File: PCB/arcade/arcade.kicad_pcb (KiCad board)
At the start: 2 copper layers, 146.3 x 55.8 mm, 55 parts, among them J1 USB_C_Receptacle_USB2.0_16P, J10 USB_A, J11 USB_A, J15 Conn_02x24_Odd_Even, J16 Conn_02x24_Odd_Even, J2 Conn_02x03_Odd_Even, J3 Conn_02x06_Odd_Even, J4 Screw_Terminal_01x02, J5 Screw_Terminal_01x12, J6 Screw_Terminal_01x08, J7 Screw_Terminal_01x12, J8 Conn_01x02_Pin, J9 Conn_01x06_Pin, U1 RP2040, U2 TLC5947RHB, U3 TLC5947RHB, U4 TLC5947RHB, U5 ME6211C33M5, U6 CD74HC4067M, U7 CD74HC4067M, U8 W25Q16JVSS, U9 FE1.1s, Y2 Crystal_GND24, Y3 Crystal_GND24

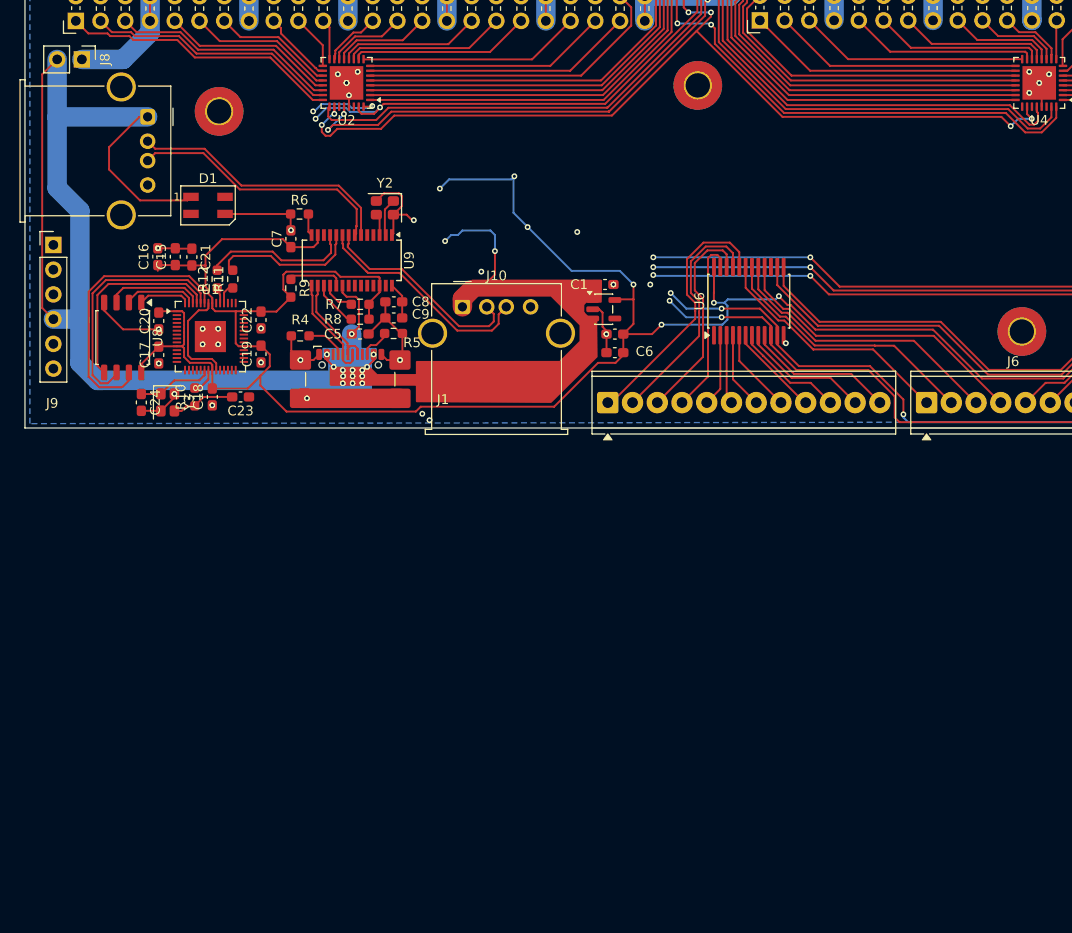
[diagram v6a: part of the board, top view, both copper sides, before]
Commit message: refactored gamepads
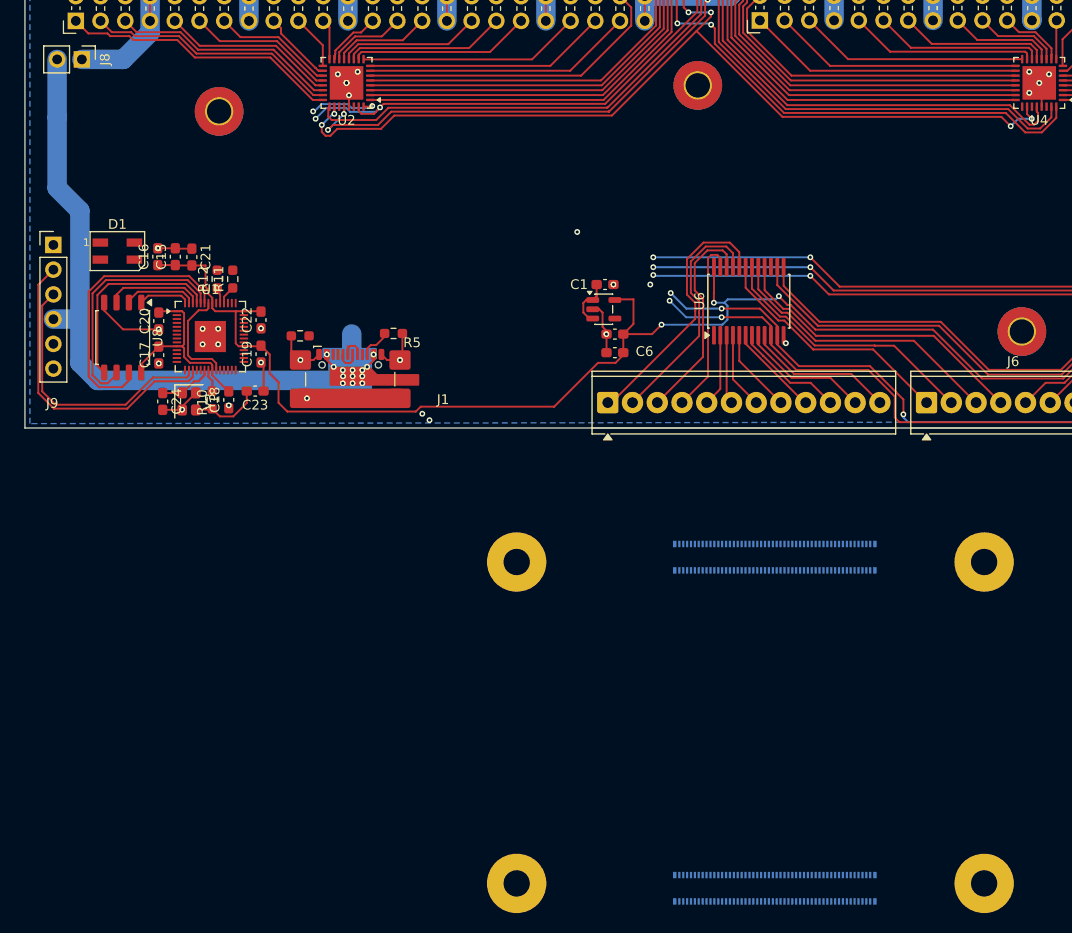
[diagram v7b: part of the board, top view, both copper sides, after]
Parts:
- removed C5, C7, C8, C9: 22pf, Capacitor_SMD:C_0603_1608Metric_Pad1.08x0.95mm_HandSolder
- removed J10, J11: USB_A, Connector_USB:USB_A_Molex_67643_Horizontal
- removed R6, R7, R8, R9: 5.1k, Resistor_SMD:R_0603_1608Metric_Pad0.98x0.95mm_HandSolder
- removed U9: FE1.1s, Package_SO:SSOP-28_3.9x9.9mm_P0.635mm
- removed Y2: Crystal_GND24, Crystal:Crystal_SMD_2520-4Pin_2.5x2.0mm
- added H5: ~, Raspberry-Pi-CM5:RaspberryPi-CM5-Module-Pad, F.Cu at (99.8, 125.5)
- moved D1 10.4 mm to (32.4, 97.0)
- moved C24 2.20 mm to (37.0, 112.5)
- moved Y3 2.20 mm to (39.7, 112.5)
- moved R10 1.81 mm to (42.1, 112.3)
- moved C18 1.71 mm to (43.8, 112.3)
- moved C23 1.62 mm to (46.5, 111.4)
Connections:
- J9 pad 2: /RXD0 -> /RX0
- J9 pad 3: /TXD0 -> /TX0
- U1 pad 16: unconnected-(U1-GPIO13-Pad16) -> /TX0
- U1 pad 17: unconnected-(U1-GPIO14-Pad17) -> /RX0
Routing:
- net /VBUS: track 147.0 -> 57.7 mm, vias 16 -> 13
- net /3.3v: track 254.6 -> 183.7 mm, vias 8 -> 4
- net /RX0: track 0.00 -> 31.9 mm
- net /TX0: track 0.00 -> 27.9 mm
- net /D3-: track 27.5 -> 0.00 mm
- net /D3+: track 26.9 -> 0.00 mm
- net /D2+: track 23.2 -> 0.00 mm
- net /GND: track 71.6 -> 49.4 mm, vias 36 -> 33
- net /D2-: track 21.6 -> 0.00 mm
- net /D1+: track 15.3 -> 0.00 mm
- net /D1-: track 14.9 -> 0.00 mm
- net /DU-: track 10.9 -> 2.46 mm
- net /DU+: track 10.9 -> 3.30 mm
- net Net-(U9-BUSJ): track 5.54 -> 0.00 mm
- net Net-(U9-~{XRSTJ}): track 4.75 -> 0.00 mm
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
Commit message: board
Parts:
- removed H5: ~, Raspberry-Pi-CM5:RaspberryPi-CM5-Module-Pad
- added Module1: ComputeModule5-CM5, Raspberry Pi CM5:Raspberry-Pi-5-Compute-Module, B.Cu at (86.4, 104.4)
- added U9: TS3USB221ARSERG4, TS3USB221A:RSE10, F.Cu at (55.8, 101.5)
- moved H3 73.1 mm to (160.8, 104.7)
- moved H1 56.8 mm to (68.5, 108.9)
- moved H2 12.6 mm to (34.1, 73.6)
- moved J2 7.91 mm to (159.8, 65.5)
- moved J4 7.91 mm to (163.0, 76.7)
- moved U2 7.91 mm to (54.5, 72.0)
- moved U3 7.91 mm to (91.0, 57.8)
- moved U4 7.91 mm to (125.6, 72.0)
- moved J15 7.91 mm to (26.7, 65.6)
- moved J8 7.91 mm to (27.3, 69.6)
- moved J16 7.91 mm to (96.9, 65.6)
- moved U5 7.67 mm to (74.6, 103.2)
- moved C1 7.67 mm to (74.8, 100.7)
- moved C2 7.67 mm to (75.8, 105.7)
- moved C6 7.67 mm to (75.8, 107.7)
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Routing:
- net Net-(J15-Pin_34): track 61.0 -> 69.6 mm
- net /VBUS: track 57.7 -> 66.0 mm
- net Net-(J6-Pin_6): track 23.0 -> 30.8 mm
- net Net-(J6-Pin_5): track 26.4 -> 34.2 mm
- net Net-(J6-Pin_7): track 20.2 -> 27.3 mm
- net /IO41: track 101.3 -> 108.4 mm
- net /EXT_5V: track 358.6 -> 365.7 mm
- net Net-(U2-SOUT): track 49.5 -> 56.6 mm
- net /3.3v: track 183.7 -> 177.0 mm, vias 4 -> 3
- net Net-(J16-Pin_37): track 17.4 -> 22.1 mm
- net /PD6: track 59.9 -> 56.9 mm
- net /PD4: track 59.0 -> 56.0 mm
- net Net-(J16-Pin_41): track 22.6 -> 25.1 mm
- net Net-(J16-Pin_43): track 25.4 -> 27.8 mm
- net Net-(J16-Pin_45): track 28.1 -> 30.4 mm
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- added copper zone on In2.Cu, net /GND
- removed copper zone on B.Cu, net /GND
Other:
- board size 146.3 x 55.8 mm -> 146.3 x 63 mm
- copper layers 2 -> 4
